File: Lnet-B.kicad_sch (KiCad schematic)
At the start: 12 parts, among them J601 RJ12, J602 RJ12, Q601 BC547, U601 LM311

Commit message: made additions to the project
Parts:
- removed D601: D, symbol Device:D
- removed J602: RJ12, symbol Connector:RJ12
- removed Q601: BC547, Package_TO_SOT_THT:TO-92_Inline, symbol Transistor_BJT:BC547
- added D1: D, Diode_SMD:D_SMA, symbol Device:D
- added J1: RJ12, Connector_RJ:RJ25_Wayconn_MJEA-660X1_Horizontal, symbol Connector:RJ12
- added Q1: AO3400A, Package_TO_SOT_SMD:SOT-23, symbol Transistor_FET:AO3400A
- D602: footprint (none) -> Diode_SMD:D_SMA; JLCPCB Part# (none) -> C14996
- J601: footprint (none) -> Connector_RJ:RJ25_Wayconn_MJEA-660X1_Horizontal; JLCPCB Part# (none) -> C77859
- R601, R602, R603, R604, R606: footprint (none) -> Resistor_SMD:R_0805_2012Metric_Pad1.20x1.40mm_HandSolder
- R605: value 1k -> 10k; footprint (none) -> Resistor_SMD:R_0805_2012Metric_Pad1.20x1.40mm_HandSolder
- U601: footprint (none) -> Package_SO:SOP-8_3.9x4.9mm_P1.27mm; JLCPCB Part# (none) -> C434495
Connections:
- net +12V: now also D1.1 (K)
- net GND: now also R605.2, J1.2, J1.5, Q1.2 (S)
- net Lnet_Tx: now also Q1.1 (G)
- net railsyncA: now also J1.6
- net railsyncB: now also D1.2 (A), J1.1
- net at J601.3, J601.4, R601.2: now also J1.3, J1.4, Q1.3 (D)
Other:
- moved on the sheet: R605

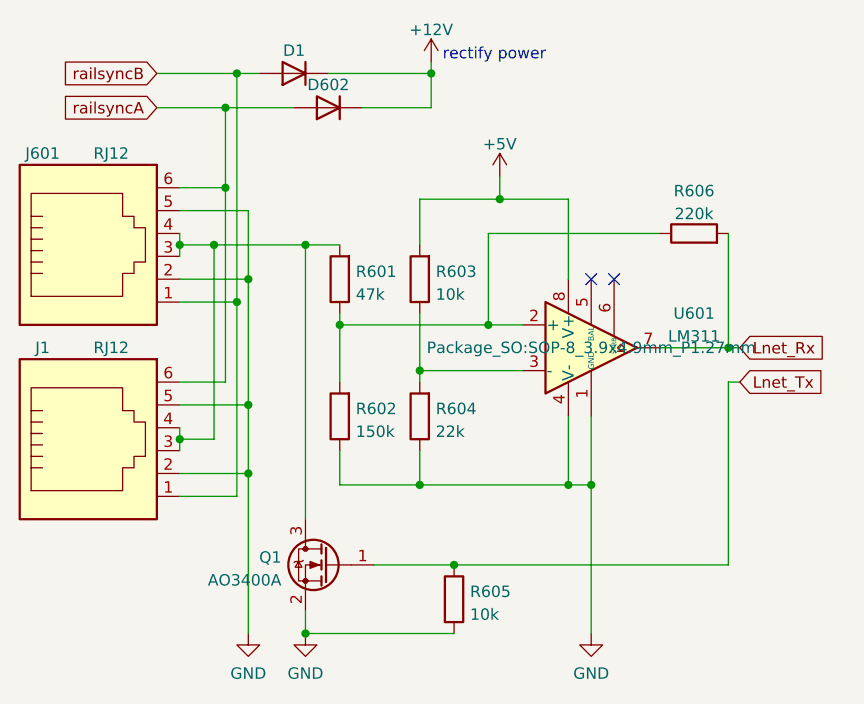
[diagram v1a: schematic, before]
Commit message: changed some stuff to ch340 and Lnet B
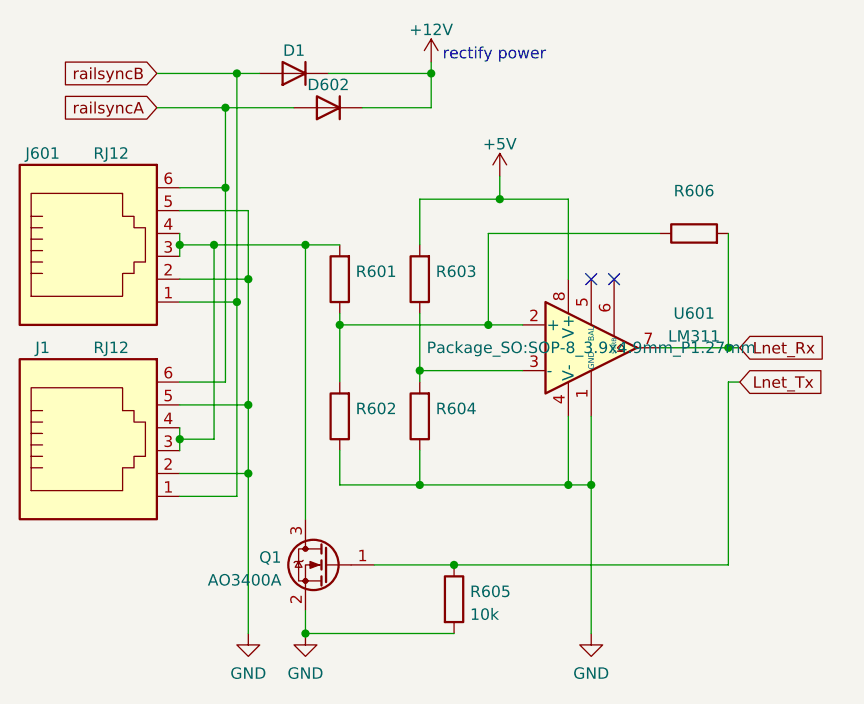
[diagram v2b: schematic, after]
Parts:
- R601: value 47k -> (none); footprint Resistor_SMD:R_0805_2012Metric_Pad1.20x1.40mm_HandSolder -> (none); JLCPCB Part# (none) -> C17713
- R602: value 150k -> (none); footprint Resistor_SMD:R_0805_2012Metric_Pad1.20x1.40mm_HandSolder -> (none); JLCPCB Part# (none) -> C17470
- R603: value 10k -> (none); footprint Resistor_SMD:R_0805_2012Metric_Pad1.20x1.40mm_HandSolder -> (none); JLCPCB Part# (none) -> C17414
- R604: value 22k -> (none); footprint Resistor_SMD:R_0805_2012Metric_Pad1.20x1.40mm_HandSolder -> (none); JLCPCB Part# (none) -> C17560
- R606: value 220k -> (none); footprint Resistor_SMD:R_0805_2012Metric_Pad1.20x1.40mm_HandSolder -> (none); JLCPCB Part# (none) -> C17556
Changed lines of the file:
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@@
       (effects (font (size 1.27 1.27)) (justify right))
     )
-    (property "Value" "150k" (id 1) (at 99.568 102.0322 0)
-      (effects (font (size 1.27 1.27)) (justify right))
-    )
-    (property "Footprint" "Resistor_SMD:R_0805_2012Metric_Pad1.20x1.40mm_HandSolder" (id 2) (at 99.568 100.33 90)
+    (property "Value" "" (id 1) (at 99.568 102.0322 0)
+      (effects (font (size 1.27 1.27)) (justify right))
+    )
+    (property "Footprint" "" (id 2) (at 99.568 100.33 90)
       (effects (font (size 1.27 1.27)) hide)
     )
@@
       (effects (font (size 1.27 1.27)) hide)
     )
+    (property "JLCPCB Part#" "C17470" (id 4) (at 97.79 100.33 0)
+      (effects (font (size 1.27 1.27)) hide)
+    )
     (pin "1")
     (pin "2")
@@
       (effects (font (size 1.27 1.27)) (justify right))
     )
-    (property "Value" "22k" (id 1) (at 108.458 102.0322 0)
-      (effects (font (size 1.27 1.27)) (justify right))
-    )
-    (property "Footprint" "Resistor_SMD:R_0805_2012Metric_Pad1.20x1.40mm_HandSolder" (id 2) (at 108.458 100.33 90)
+    (property "Value" "" (id 1) (at 108.458 102.0322 0)
+      (effects (font (size 1.27 1.27)) (justify right))
+    )
+    (property "Footprint" "" (id 2) (at 108.458 100.33 90)
       (effects (font (size 1.27 1.27)) hide)
     )
@@
       (effects (font (size 1.27 1.27)) hide)
     )
+    (property "JLCPCB Part#" "C17560" (id 4) (at 106.68 100.33 0)
+      (effects (font (size 1.27 1.27)) hide)
+    )
     (pin "1")
     (pin "2")
@@
       (effects (font (size 1.27 1.27)) (justify right))
     )
-    (property "Value" "47k" (id 1) (at 99.568 86.7922 0)
-      (effects (font (size 1.27 1.27)) (justify right))
-    )
-    (property "Footprint" "Resistor_SMD:R_0805_2012Metric_Pad1.20x1.40mm_HandSolder" (id 2) (at 99.568 85.09 90)
+    (property "Value" "" (id 1) (at 99.568 86.7922 0)
+      (effects (font (size 1.27 1.27)) (justify right))
+    )
+    (property "Footprint" "" (id 2) (at 99.568 85.09 90)
       (effects (font (size 1.27 1.27)) hide)
     )
     (property "Datasheet" "~" (id 3) (at 97.79 85.09 0)
+      (effects (font (size 1.27 1.27)) hide)
+    )
+    (property "JLCPCB Part#" "C17713" (id 4) (at 97.79 85.09 0)
       (effects (font (size 1.27 1.27)) hide)
     )
@@
       (effects (font (size 1.27 1.27)) (justify right))
     )
-    (property "Value" "10k" (id 1) (at 108.458 86.7922 0)
-      (effects (font (size 1.27 1.27)) (justify right))
-    )
-    (property "Footprint" "Resistor_SMD:R_0805_2012Metric_Pad1.20x1.40mm_HandSolder" (id 2) (at 108.458 85.09 90)
+    (property "Value" "" (id 1) (at 108.458 86.7922 0)
+      (effects (font (size 1.27 1.27)) (justify right))
+    )
+    (property "Footprint" "" (id 2) (at 108.458 85.09 90)
       (effects (font (size 1.27 1.27)) hide)
     )
     (property "Datasheet" "~" (id 3) (at 106.68 85.09 0)
+      (effects (font (size 1.27 1.27)) hide)
+    )
+    (property "JLCPCB Part#" "C17414" (id 4) (at 106.68 85.09 0)
       (effects (font (size 1.27 1.27)) hide)
     )
@@
     (in_bom yes) (on_board yes) (fields_autoplaced)
     (property "Reference" "R606" (id 0) (at 137.16 75.2942 90))
-    (property "Value" "220k" (id 1) (at 137.16 77.8311 90))
-    (property "Footprint" "Resistor_SMD:R_0805_2012Metric_Pad1.20x1.40mm_HandSolder" (id 2) (at 137.16 81.788 90)
+    (property "Value" "" (id 1) (at 137.16 77.8311 90))
+    (property "Footprint" "" (id 2) (at 137.16 81.788 90)
       (effects (font (size 1.27 1.27)) hide)
     )
@@
       (effects (font (size 1.27 1.27)) hide)
     )
+    (property "JLCPCB Part#" "C17556" (id 4) (at 137.16 80.01 90)
+      (effects (font (size 1.27 1.27)) hide)
+    )

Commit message: added decoupling capacitor to atmega schematic
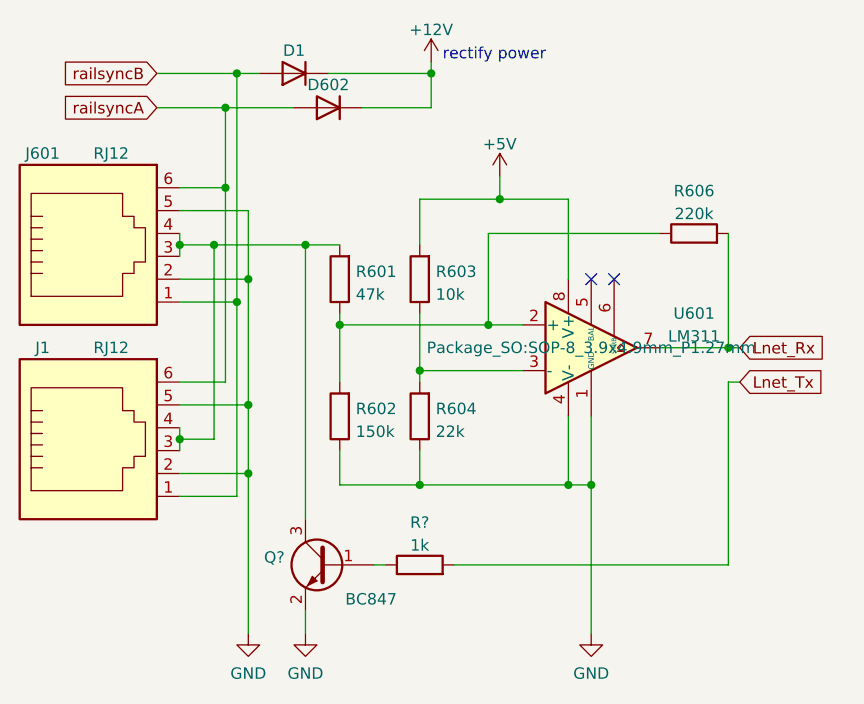
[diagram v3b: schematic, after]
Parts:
- removed Q1: AO3400A, Package_TO_SOT_SMD:SOT-23, symbol Transistor_FET:AO3400A
- removed R605: 10k, Resistor_SMD:R_0805_2012Metric_Pad1.20x1.40mm_HandSolder, symbol Device:R
- added Q?: BC847, Package_TO_SOT_SMD:SOT-23, symbol Transistor_BJT:BC847
- added R?: 1k, Resistor_SMD:R_0603_1608Metric_Pad0.98x0.95mm_HandSolder, symbol Device:R
- R601: value (none) -> 47k; footprint (none) -> Resistor_SMD:R_0805_2012Metric_Pad1.20x1.40mm_HandSolder
- R602: value (none) -> 150k; footprint (none) -> Resistor_SMD:R_0805_2012Metric_Pad1.20x1.40mm_HandSolder
- R603: value (none) -> 10k; footprint (none) -> Resistor_SMD:R_0805_2012Metric_Pad1.20x1.40mm_HandSolder
- R604: value (none) -> 22k; footprint (none) -> Resistor_SMD:R_0805_2012Metric_Pad1.20x1.40mm_HandSolder
- R606: value (none) -> 220k; footprint (none) -> Resistor_SMD:R_0805_2012Metric_Pad1.20x1.40mm_HandSolder
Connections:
- net GND: now also Q?.2 (E)
- net Lnet_Tx: now also R?.2
- net at J1.3, J1.4, J601.3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: now also Q?.3 (C)
- new net: Q?.1 (B), R?.1
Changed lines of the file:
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@@
   (junction (at 140.97 92.71) (diameter 0) (color 0 0 0 0)
   )
-  (junction (at 93.98 124.46) (diameter 0) (color 0 0 0 0)
-  )
   (junction (at 80.01 102.87) (diameter 0) (color 0 0 0 0)
   )
@@
   )
   (junction (at 87.63 106.68) (diameter 0) (color 0 0 0 0)
-  )
-  (junction (at 110.49 116.84) (diameter 0) (color 0 0 0 0)
   )
   (junction (at 85.09 74.93) (diameter 0) (color 0 0 0 0)
@@
     (stroke (width 0) (type default) (color 0 0 0 0))
   )
+  (wire (pts (xy 110.49 116.84) (xy 140.97 116.84))
+    (stroke (width 0) (type default) (color 0 0 0 0))
+  )
   (wire (pts (xy 123.19 85.09) (xy 123.19 76.2))
     (stroke (width 0) (type default) (color 0 0 0 0))
@@
     (stroke (width 0) (type default) (color 0 0 0 0))
   )
-  (wire (pts (xy 110.49 116.84) (xy 140.97 116.84))
-    (stroke (width 0) (type default) (color 0 0 0 0))
-  )
   (wire (pts (xy 140.97 92.71) (xy 133.35 92.71))
     (stroke (width 0) (type default) (color 0 0 0 0))
@@
     (stroke (width 0) (type default) (color 0 0 0 0))
   )
-  (wire (pts (xy 93.98 124.46) (xy 110.49 124.46))
-    (stroke (width 0) (type default) (color 0 0 0 0))
-  )
   (wire (pts (xy 80.01 102.87) (xy 80.01 104.14))
     (stroke (width 0) (type default) (color 0 0 0 0))
@@
     (stroke (width 0) (type default) (color 0 0 0 0))
   )
-  (wire (pts (xy 101.6 116.84) (xy 110.49 116.84))
+  (wire (pts (xy 101.6 116.84) (xy 102.87 116.84))
     (stroke (width 0) (type default) (color 0 0 0 0))
   )
@@
     )
     (pin "1")
+  )
+  (symbol (lib_id "Device:R") (at 106.68 116.84 90) (unit 1)
+    (in_bom yes) (on_board yes) (fields_autoplaced)
+    (property "Reference" "R?" (id 0) (at 106.68 112.1242 90))
+    (property "Value" "1k" (id 1) (at 106.68 114.6611 90))
+    (property "Footprint" "Resistor_SMD:R_0603_1608Metric_Pad0.98x0.95mm_HandSolder" (id 2) (at 106.68 118.618 90)
+      (effects (font (size 1.27 1.27)) hide)
+    )
+    (property "Datasheet" "~" (id 3) (at 106.68 116.84 0)
+      (effects (font (size 1.27 1.27)) hide)
+    )
+    (property "JLCPCB Part#" "C21190" (id 4) (at 106.68 116.84 90)
+      (effects (font (size 1.27 1.27)) hide)
+    )
+    (pin "1")
+    (pin "2")
   )
   (symbol (lib_id "Comparator:LM311") (at 125.73 92.71 0) (unit 1)
@@
       (effects (font (size 1.27 1.27)) (justify right))
     )
-    (property "Value" "" (id 1) (at 99.568 102.0322 0)
-      (effects (font (size 1.27 1.27)) (justify right))
-    )
-    (property "Footprint" "" (id 2) (at 99.568 100.33 90)
+    (property "Value" "150k" (id 1) (at 99.568 102.0322 0)
+      (effects (font (size 1.27 1.27)) (justify right))
+    )
+    (property "Footprint" "Resistor_SMD:R_0805_2012Metric_Pad1.20x1.40mm_HandSolder" (id 2) (at 99.568 100.33 90)
       (effects (font (size 1.27 1.27)) hide)
     )
@@
       (effects (font (size 1.27 1.27)) (justify right))
     )
-    (property "Value" "" (id 1) (at 108.458 102.0322 0)
-      (effects (font (size 1.27 1.27)) (justify right))
-    )
-    (property "Footprint" "" (id 2) (at 108.458 100.33 90)
+    (property "Value" "22k" (id 1) (at 108.458 102.0322 0)
+      (effects (font (size 1.27 1.27)) (justify right))
+    )
+    (property "Footprint" "Resistor_SMD:R_0805_2012Metric_Pad1.20x1.40mm_HandSolder" (id 2) (at 108.458 100.33 90)
       (effects (font (size 1.27 1.27)) hide)
     )
@@
       (effects (font (size 1.27 1.27)) (justify right))
     )
-    (property "Value" "" (id 1) (at 99.568 86.7922 0)
-      (effects (font (size 1.27 1.27)) (justify right))
-    )
-    (property "Footprint" "" (id 2) (at 99.568 85.09 90)
+    (property "Value" "47k" (id 1) (at 99.568 86.7922 0)
+      (effects (font (size 1.27 1.27)) (justify right))
+    )
+    (property "Footprint" "Resistor_SMD:R_0805_2012Metric_Pad1.20x1.40mm_HandSolder" (id 2) (at 99.568 85.09 90)
       (effects (font (size 1.27 1.27)) hide)
     )
@@
     (pin "2")
   )
-  (symbol (lib_id "Device:R") (at 110.49 120.65 0) (unit 1)
-    (in_bom yes) (on_board yes) (fields_autoplaced)
-    (property "Reference" "R605" (id 0) (at 112.268 119.8153 0)
+  (symbol (lib_id "Transistor_BJT:BC847") (at 96.52 116.84 0) (mirror y) (unit 1)
+    (in_bom yes) (on_board yes)
+    (property "Reference" "Q?" (id 0) (at 91.6686 116.0053 0)
       (effects (font (size 1.27 1.27)) (justify left))
     )
-    (property "Value" "10k" (id 1) (at 112.268 122.3522 0)
-      (effects (font (size 1.27 1.27)) (justify left))
-    )
-    (property "Footprint" "Resistor_SMD:R_0805_2012Metric_Pad1.20x1.40mm_HandSolder" (id 2) (at 108.712 120.65 90)
-      (effects (font (size 1.27 1.27)) hide)
-    )
-    (property "Datasheet" "~" (id 3) (at 110.49 120.65 0)
-      (effects (font (size 1.27 1.27)) hide)
-    )
-    (pin "1")
-    (pin "2")
-  )
-  (symbol (lib_id "Transistor_FET:AO3400A") (at 96.52 116.84 0) (mirror y) (unit 1)
-    (in_bom yes) (on_board yes) (fields_autoplaced)
-    (property "Reference" "Q1" (id 0) (at 91.3131 116.0053 0)
-      (effects (font (size 1.27 1.27)) (justify left))
-    )
-    (property "Value" "AO3400A" (id 1) (at 91.3131 118.5422 0)
+    (property "Value" "BC847" (id 1) (at 104.14 120.65 0)
       (effects (font (size 1.27 1.27)) (justify left))
     )
@@
       (effects (font (size 1.27 1.27) italic) (justify left) hide)
     )
-    (property "Datasheet" "http://www.aosmd.com/pdfs/datasheet/AO3400A.pdf" (id 3) (at 96.52 116.84 0)
+    (property "Datasheet" "http://www.infineon.com/dgdl/Infineon-BC847SERIES_BC848SERIES_BC849SERIES_BC850SERIES-DS-v01_01-en.pdf?fileId=db3a304314dca389011541d4630a1657" (id 3) (at 96.52 116.84 0)
       (effects (font (size 1.27 1.27)) (justify left) hide)
     )
-    (property "JLCPCB Part#" "C20917" (id 4) (at 96.52 116.84 0)
+    (property "JLCPCB Part#" "C181140" (id 4) (at 96.52 116.84 0)
       (effects (font (size 1.27 1.27)) hide)
     )
@@
       (effects (font (size 1.27 1.27)) (justify right))
     )
-    (property "Value" "" (id 1) (at 108.458 86.7922 0)
-      (effects (font (size 1.27 1.27)) (justify right))
-    )
-    (property "Footprint" "" (id 2) (at 108.458 85.09 90)
+    (property "Value" "10k" (id 1) (at 108.458 86.7922 0)
+      (effects (font (size 1.27 1.27)) (justify right))
+    )
+    (property "Footprint" "Resistor_SMD:R_0805_2012Metric_Pad1.20x1.40mm_HandSolder" (id 2) (at 108.458 85.09 90)
       (effects (font (size 1.27 1.27)) hide)
     )
@@
     (in_bom yes) (on_board yes) (fields_autoplaced)
     (property "Reference" "R606" (id 0) (at 137.16 75.2942 90))
-    (property "Value" "" (id 1) (at 137.16 77.8311 90))
-    (property "Footprint" "" (id 2) (at 137.16 81.788 90)
-      (effects (font (size 1.27 1.27)) hide)
-    )
+    (property "Value" "220k" (id 1) (at 137.16 77.8311 90))
+    (property "Footprint" "Resistor_SMD:R_0805_2012Metric_Pad1.20x1.40mm_HandSolder" (id 2) (at 137.16 81.788 90)
+      (effects (font (size 1.27 1.27)) hide)
+    )

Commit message: added hierarchial labels to some schematics
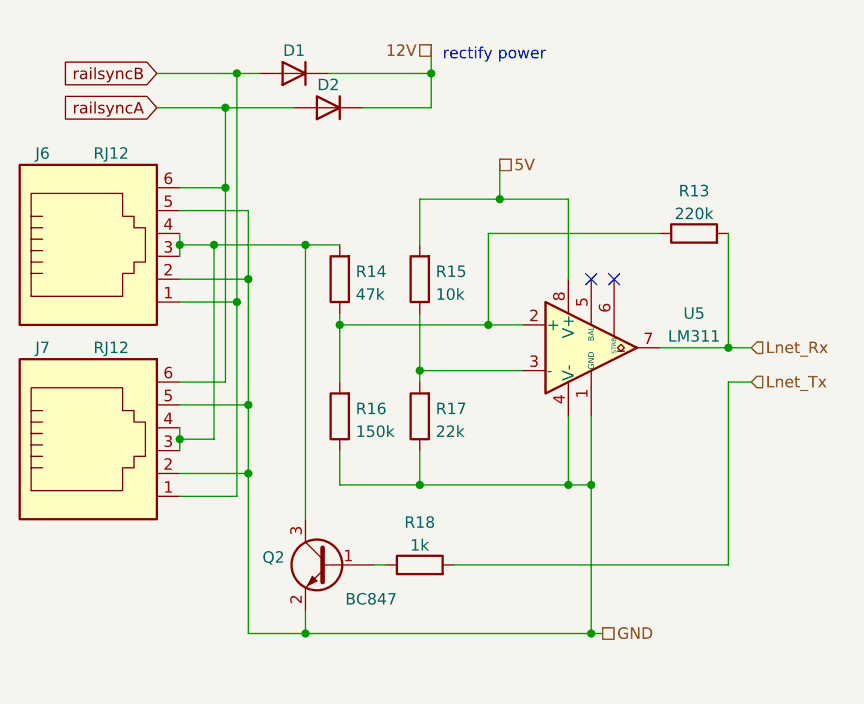
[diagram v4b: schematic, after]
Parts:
- gave numbers to parts that had none: 2
- renumbered D602 to D2, J601 to J6, J1 to J7, R606 to R13, R601 to R14, R603 to R15, R602 to R16, R604 to R17, U601 to U5
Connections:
- net +12V renamed 12V
- net +5V renamed 5V
